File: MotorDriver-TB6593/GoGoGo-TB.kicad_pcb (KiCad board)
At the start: 2 copper layers, 25.4 x 27.9 mm, 21 parts, among them P1 CONN_01X03, P2 CONN_01X04, P3 CONN_01X02, U1 TB6593FNG

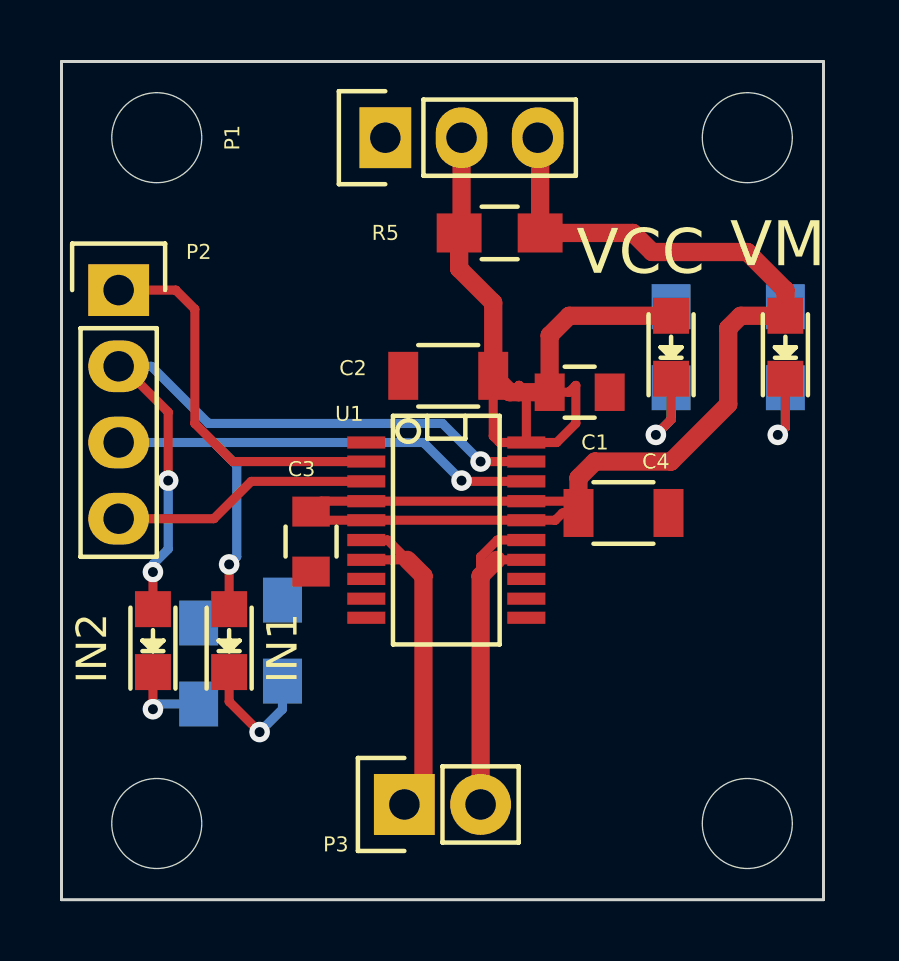
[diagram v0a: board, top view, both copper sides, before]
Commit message: Added via footprint and stitched the planes together.
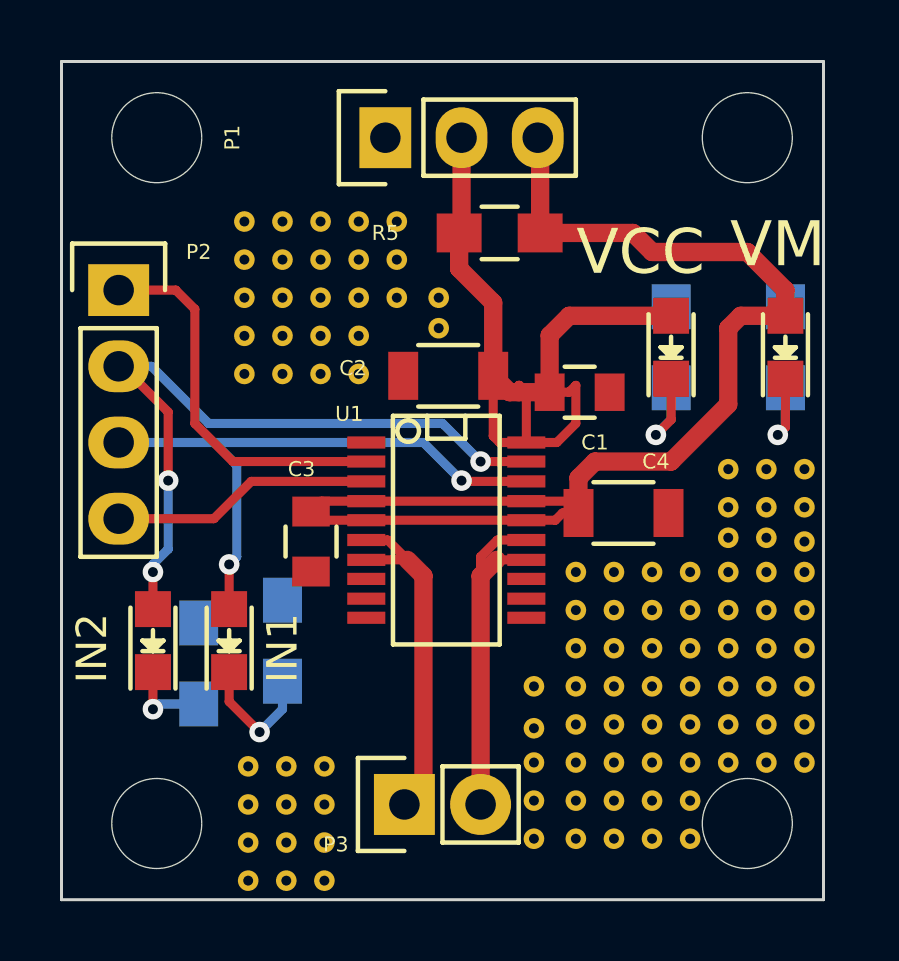
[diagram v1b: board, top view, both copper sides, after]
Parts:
- added REF**111: Via, MotorDriver:Via, F.Cu at (157.5, 110.5)
- added REF**112: Via, MotorDriver:Via, F.Cu at (157.5, 111.8)
- added REF**113: Via, MotorDriver:Via, F.Cu at (157.5, 113.0)
- added REF**114: Via, MotorDriver:Via, F.Cu at (157.5, 114.3)
- added REF**115: Via, MotorDriver:Via, F.Cu at (157.5, 115.6)
- added REF**121: Via, MotorDriver:Via, F.Cu at (158.8, 110.5)
- added REF**122: Via, MotorDriver:Via, F.Cu at (158.8, 111.8)
- added REF**123: Via, MotorDriver:Via, F.Cu at (158.8, 113.0)
- added REF**124: Via, MotorDriver:Via, F.Cu at (158.8, 114.3)
- added REF**125: Via, MotorDriver:Via, F.Cu at (158.8, 115.6)
- added REF**131: Via, MotorDriver:Via, F.Cu at (160.0, 110.5)
- added REF**132: Via, MotorDriver:Via, F.Cu at (160.0, 111.8)
- added REF**133: Via, MotorDriver:Via, F.Cu at (160.0, 113.0)
- added REF**134: Via, MotorDriver:Via, F.Cu at (160.0, 114.3)
- added REF**135: Via, MotorDriver:Via, F.Cu at (160.0, 115.6)
- added REF**141: Via, MotorDriver:Via, F.Cu at (161.3, 110.5)
- added REF**142: Via, MotorDriver:Via, F.Cu at (161.3, 111.8)
- added REF**143: Via, MotorDriver:Via, F.Cu at (161.3, 113.0)
- added REF**144: Via, MotorDriver:Via, F.Cu at (161.3, 114.3)
- added REF**145: Via, MotorDriver:Via, F.Cu at (161.3, 115.6)
- added REF**151: Via, MotorDriver:Via, F.Cu at (162.6, 110.5)
- added REF**1511: Via, MotorDriver:Via, F.Cu at (168.5, 122.2)
- added REF**1512: Via, MotorDriver:Via, F.Cu at (168.5, 123.4)
- added REF**1513: Via, MotorDriver:Via, F.Cu at (168.5, 124.7)
- added REF**1514: Via, MotorDriver:Via, F.Cu at (168.5, 126.0)
- added REF**1515: Via, MotorDriver:Via, F.Cu at (168.5, 127.3)
- added REF**1516: Via, MotorDriver:Via, F.Cu at (168.5, 128.5)
- added REF**1517: Via, MotorDriver:Via, F.Cu at (168.5, 129.8)
- added REF**1518: Via, MotorDriver:Via, F.Cu at (168.5, 131.1)
- added REF**152: Via, MotorDriver:Via, F.Cu at (162.6, 111.8)
- added REF**1521: Via, MotorDriver:Via, F.Cu at (169.8, 122.2)
- added REF**1522: Via, MotorDriver:Via, F.Cu at (169.8, 123.4)
- added REF**1523: Via, MotorDriver:Via, F.Cu at (169.8, 124.7)
- added REF**1524: Via, MotorDriver:Via, F.Cu at (169.8, 126.0)
- added REF**1525: Via, MotorDriver:Via, F.Cu at (169.8, 127.3)
- added REF**1526: Via, MotorDriver:Via, F.Cu at (169.8, 128.5)
- added REF**1527: Via, MotorDriver:Via, F.Cu at (169.8, 129.8)
- added REF**1528: Via, MotorDriver:Via, F.Cu at (169.8, 131.1)
- added REF**153: Via, MotorDriver:Via, F.Cu at (162.6, 113.0)
- added REF**1531: Via, MotorDriver:Via, F.Cu at (171.1, 122.2)
- added REF**1532: Via, MotorDriver:Via, F.Cu at (171.1, 123.4)
- added REF**1533: Via, MotorDriver:Via, F.Cu at (171.1, 124.7)
- added REF**1534: Via, MotorDriver:Via, F.Cu at (171.1, 126.0)
- added REF**1535: Via, MotorDriver:Via, F.Cu at (171.1, 127.3)
- added REF**1536: Via, MotorDriver:Via, F.Cu at (171.1, 128.5)
- added REF**1537: Via, MotorDriver:Via, F.Cu at (171.1, 129.8)
- added REF**1538: Via, MotorDriver:Via, F.Cu at (171.1, 131.1)
- added REF**154: Via, MotorDriver:Via, F.Cu at (164.0, 114.0)
- added REF**1541: Via, MotorDriver:Via, F.Cu at (172.3, 122.2)
- added REF**1542: Via, MotorDriver:Via, F.Cu at (172.3, 123.4)
- added REF**1543: Via, MotorDriver:Via, F.Cu at (172.3, 124.7)
- added REF**1544: Via, MotorDriver:Via, F.Cu at (172.3, 126.0)
- added REF**1545: Via, MotorDriver:Via, F.Cu at (172.3, 127.3)
- added REF**1546: Via, MotorDriver:Via, F.Cu at (172.3, 128.5)
- added REF**1547: Via, MotorDriver:Via, F.Cu at (172.3, 129.8)
- added REF**1548: Via, MotorDriver:Via, F.Cu at (172.3, 131.1)
- added REF**155: Via, MotorDriver:Via, F.Cu at (164.0, 113.0)
- added REF**1551: Via, MotorDriver:Via, F.Cu at (173.6, 122.2)
- added REF**155111: Via, MotorDriver:Via, F.Cu at (157.6, 128.7)
- added REF**155112: Via, MotorDriver:Via, F.Cu at (157.6, 129.9)
- added REF**155113: Via, MotorDriver:Via, F.Cu at (157.6, 131.2)
- added REF**155114: Via, MotorDriver:Via, F.Cu at (157.6, 132.5)
- added REF**155121: Via, MotorDriver:Via, F.Cu at (158.9, 128.7)
- added REF**155122: Via, MotorDriver:Via, F.Cu at (158.9, 129.9)
- added REF**155123: Via, MotorDriver:Via, F.Cu at (158.9, 131.2)
- added REF**155124: Via, MotorDriver:Via, F.Cu at (158.9, 132.5)
- added REF**155131: Via, MotorDriver:Via, F.Cu at (160.1, 128.7)
- added REF**155132: Via, MotorDriver:Via, F.Cu at (160.1, 129.9)
- added REF**155133: Via, MotorDriver:Via, F.Cu at (160.1, 131.2)
- added REF**155134: Via, MotorDriver:Via, F.Cu at (160.1, 132.5)
- added REF**1552: Via, MotorDriver:Via, F.Cu at (173.6, 123.4)
- added REF**1553: Via, MotorDriver:Via, F.Cu at (173.6, 124.7)
- added REF**1554: Via, MotorDriver:Via, F.Cu at (173.6, 126.0)
- added REF**1555: Via, MotorDriver:Via, F.Cu at (173.6, 127.3)
- added REF**1556: Via, MotorDriver:Via, F.Cu at (173.6, 128.5)
- added REF**1557: Via, MotorDriver:Via, F.Cu at (167.1, 129.8)
- added REF**1558: Via, MotorDriver:Via, F.Cu at (167.1, 131.1)
- added REF**1561: Via, MotorDriver:Via, F.Cu at (174.9, 122.2)
- added REF**1562: Via, MotorDriver:Via, F.Cu at (174.9, 123.4)
- added REF**1563: Via, MotorDriver:Via, F.Cu at (174.9, 124.7)
- added REF**1564: Via, MotorDriver:Via, F.Cu at (174.9, 126.0)
- added REF**1565: Via, MotorDriver:Via, F.Cu at (174.9, 127.3)
- added REF**1566: Via, MotorDriver:Via, F.Cu at (174.9, 128.5)
- added REF**1567: Via, MotorDriver:Via, F.Cu at (167.1, 128.5)
- added REF**1568: Via, MotorDriver:Via, F.Cu at (167.1, 127.4)
- added REF**1571: Via, MotorDriver:Via, F.Cu at (176.1, 122.2)
- added REF**1572: Via, MotorDriver:Via, F.Cu at (176.1, 123.4)
- added REF**1573: Via, MotorDriver:Via, F.Cu at (176.1, 124.7)
- added REF**1574: Via, MotorDriver:Via, F.Cu at (176.1, 126.0)
- added REF**1575: Via, MotorDriver:Via, F.Cu at (176.1, 127.3)
- added REF**1576: Via, MotorDriver:Via, F.Cu at (176.1, 128.5)
- added REF**1577: Via, MotorDriver:Via, F.Cu at (167.1, 126.0)
- added REF**1578: Via, MotorDriver:Via, F.Cu at (173.6, 118.7)
- added REF**1581: Via, MotorDriver:Via, F.Cu at (173.6, 121.0)
- added REF**1582: Via, MotorDriver:Via, F.Cu at (174.9, 121.0)
- added REF**1583: Via, MotorDriver:Via, F.Cu at (176.1, 121.2)
- added REF**1584: Via, MotorDriver:Via, F.Cu at (176.1, 120.0)
- added REF**1585: Via, MotorDriver:Via, F.Cu at (174.9, 120.0)
- added REF**1586: Via, MotorDriver:Via, F.Cu at (173.6, 120.0)
- added REF**1587: Via, MotorDriver:Via, F.Cu at (174.9, 118.7)
- added REF**1588: Via, MotorDriver:Via, F.Cu at (176.1, 118.7)
- renumbered REF** to REF**11

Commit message: Did DRC and added silkscreen
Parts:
- moved REF**1566 14.0 mm to (161.3, 125.0)
- moved REF**1576 13.8 mm to (162.4, 127.3)
- moved REF**1548 12.1 mm to (161.3, 126.1)
- moved REF**1556 11.4 mm to (162.4, 126.1)
- moved REF**1547 11.3 mm to (161.3, 127.3)
- moved REF**1546 10.5 mm to (162.4, 125.0)
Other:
- board text added: "G"
- board text added: "PWM"
- board text added: "STBY"
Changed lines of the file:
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@@
 (kicad_pcb (version 4) (host pcbnew 0.201509151501+6198~30~ubuntu14.04.1-product)
   (general
-    (links 132)
+    (links 143)
     (no_connects 0)
     (area 150.669934 103.0431 179.054303 136.10966)
     (thickness 1.6)
-    (drawings 8)
+    (drawings 13)
     (tracks 113)
     (zones 0)
@@
   (layers
     (0 F.Cu signal)
-    (31 B.Cu signal)
-    (32 B.Adhes user)
+    (31 B.Cu signal hide)
+    (32 B.Adhes user hide)
     (33 F.Adhes user)
-    (34 B.Paste user)
+    (34 B.Paste user hide)
     (35 F.Paste user)
-    (36 B.SilkS user)
+    (36 B.SilkS user hide)
     (37 F.SilkS user)
     (38 B.Mask user)
@@
   )
   (setup
-    (last_trace_width 0.1524)
+    (last_trace_width 0.6096)
     (user_trace_width 0.3048)
     (user_trace_width 0.6096)
@@
     (aux_axis_origin 0 0)
     (grid_origin 161.544 117.856)
-    (visible_elements FFFEFF7F)
+    (visible_elements FFFEFB3F)
     (pcbplotparams
       (layerselection 0x010fc_80000001)
@@
   )
   (module MotorDriver:Via (layer F.Cu)
-    (at 172.339 131.064)
+    (at 161.29 126.111)
     (fp_text reference REF**1548 (at 0 1) (layer F.SilkS) hide
       (effects (font (size 1 1) (thickness 0.15)))
@@
   )
   (module MotorDriver:Via (layer F.Cu)
-    (at 172.339 129.794)
+    (at 161.29 127.254)
     (fp_text reference REF**1547 (at 0 1) (layer F.SilkS) hide
       (effects (font (size 1 1) (thickness 0.15)))
@@
   )
   (module MotorDriver:Via (layer F.Cu)
-    (at 176.149 128.524)
+    (at 162.433 127.254)
     (fp_text reference REF**1576 (at 0 1) (layer F.SilkS) hide
       (effects (font (size 1 1) (thickness 0.15)))
@@
   )
   (module MotorDriver:Via (layer F.Cu)
-    (at 174.879 128.524)
+    (at 161.29 124.968)
     (fp_text reference REF**1566 (at 0 1) (layer F.SilkS) hide
       (effects (font (size 1 1) (thickness 0.15)))
@@
   )
   (module MotorDriver:Via (layer F.Cu)
-    (at 173.609 128.524)
+    (at 162.433 126.111)
     (fp_text reference REF**1556 (at 0 1) (layer F.SilkS) hide
       (effects (font (size 1 1) (thickness 0.15)))
@@
   )
   (module MotorDriver:Via (layer F.Cu)
-    (at 172.339 128.524)
+    (at 162.433 124.968)
     (fp_text reference REF**1546 (at 0 1) (layer F.SilkS) hide
       (effects (font (size 1 1) (thickness 0.15)))
@@
     (tags "capacitor 1206")
     (attr smd)
-    (fp_text reference C4 (at 1.0795 -1.7145) (layer F.SilkS)
+    (fp_text reference C4 (at 2.2225 -1.8415) (layer F.SilkS)
       (effects (font (size 0.5 0.5) (thickness 0.1)))
     )
@@
     (tags "capacitor 0805")
     (attr smd)
-    (fp_text reference C1 (at 0.508 1.6764) (layer F.SilkS)
+    (fp_text reference C1 (at 0.635 -1.4986) (layer F.SilkS)
       (effects (font (size 0.5 0.5) (thickness 0.1)))
     )
@@
     (tags "capacitor 1206")
     (attr smd)
-    (fp_text reference C2 (at 3.175 0.254 180) (layer F.SilkS)
+    (fp_text reference C2 (at 1.5875 1.7145 180) (layer F.SilkS)
       (effects (font (size 0.5 0.5) (thickness 0.1)))
     )
@@
     (descr "Through hole pin header")
     (tags "pin header")
-    (fp_text reference P2 (at 2.667 -1.27) (layer F.SilkS)
+    (fp_text reference P2 (at -1.27 -2.286) (layer F.SilkS)
       (effects (font (size 0.5 0.5) (thickness 0.1)))
     )
@@
     (tags "CMS SSOP SMD")
     (attr smd)
-    (fp_text reference U1 (at -3.8735 3.2385 360) (layer F.SilkS)
+    (fp_text reference U1 (at -3.302 2.54 360) (layer F.SilkS)
       (effects (font (size 0.5 0.5) (thickness 0.1)))
     )
@@
       (net 1 GND) (zone_connect 2))
   )
-  (gr_text IN1 (at 158.75 124.714 90) (layer F.SilkS)
+  (gr_text PWM (at 156.591 113.157) (layer F.SilkS)
+    (effects (font (size 0.762 0.762) (thickness 0.1524)))
+  )
+  (gr_text IN2 (at 155.829 115.443) (layer F.SilkS)
+    (effects (font (size 0.762 0.762) (thickness 0.1524)))
+  )
+  (gr_text IN1 (at 156.083 117.729) (layer F.SilkS)
+    (effects (font (size 0.762 0.762) (thickness 0.1524)))
+  )
+  (gr_text STBY (at 156.21 120.396) (layer F.SilkS)
+    (effects (font (size 0.762 0.762) (thickness 0.1524)))
+  )
+  (gr_text G (at 159.639 108.077) (layer F.SilkS)
+    (effects (font (size 1.016 1.016) (thickness 0.2032)))
+  )
+  (gr_text IN1 (at 158.75 124.46 90) (layer F.SilkS)
     (effects (font (size 1.016 1.016) (thickness 0.2032)))
   )
@@
     (effects (font (size 1.016 1.016) (thickness 0.2032)))
   )
-  (gr_text VM (at 175.26 111.252) (layer F.SilkS)
-    (effects (font (size 1.5 1.5) (thickness 0.3)))
-  )
-  (gr_text VCC (at 170.688 111.506) (layer F.SilkS)
-    (effects (font (size 1.5 1.5) (thickness 0.3)))
+  (gr_text VM (at 175.514 111.633) (layer F.SilkS)
+    (effects (font (size 1.016 1.016) (thickness 0.2032)))
+  )
+  (gr_text VCC (at 171.45 111.506) (layer F.SilkS)
+    (effects (font (size 1.016 1.016) (thickness 0.2032)))
   )
   (gr_line (start 151.384 133.096) (end 176.784 133.096) (layer Edge.Cuts) (width 0.1))

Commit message: Added previous commit # for tracking PCBs
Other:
- board text added: "GoGoGo Motor Driver Board Commit #: b2918eb"
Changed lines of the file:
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@@
     (links 143)
     (no_connects 0)
-    (area 150.669934 103.0431 179.054303 136.10966)
+    (area 150.669934 103.0431 180.42402 136.10966)
     (thickness 1.6)
-    (drawings 13)
+    (drawings 14)
     (tracks 113)
     (zones 0)
@@
   (page A4)
   (layers
-    (0 F.Cu signal)
-    (31 B.Cu signal hide)
-    (32 B.Adhes user hide)
-    (33 F.Adhes user)
-    (34 B.Paste user hide)
-    (35 F.Paste user)
-    (36 B.SilkS user hide)
-    (37 F.SilkS user)
+    (0 F.Cu signal hide)
+    (31 B.Cu signal)
+    (32 B.Adhes user)
+    (33 F.Adhes user hide)
+    (34 B.Paste user)
+    (35 F.Paste user hide)
+    (36 B.SilkS user)
+    (37 F.SilkS user hide)
     (38 B.Mask user)
-    (39 F.Mask user)
-    (40 Dwgs.User user)
+    (39 F.Mask user hide)
+    (40 Dwgs.User user hide)
     (41 Cmts.User user)
     (42 Eco1.User user)
@@
   )
   (setup
-    (last_trace_width 0.6096)
+    (last_trace_width 0.1524)
     (user_trace_width 0.3048)
     (user_trace_width 0.6096)
@@
     (aux_axis_origin 0 0)
     (grid_origin 161.544 117.856)
-    (visible_elements FFFEFB3F)
+    (visible_elements FFFEBD5F)
     (pcbplotparams
       (layerselection 0x010fc_80000001)
@@
     (tags "resistor 0805")
     (attr smd)
-    (fp_text reference R1 (at 0 2.1 270) (layer B.SilkS)
+    (fp_text reference R1 (at 1.778 1.397 270) (layer B.SilkS)
       (effects (font (size 0.5 0.5) (thickness 0.1)) (justify mirror))
     )
@@
     (tags "resistor 0805")
     (attr smd)
-    (fp_text reference R2 (at 0 2.1 270) (layer B.SilkS)
+    (fp_text reference R2 (at 1.905 1.651 270) (layer B.SilkS)
       (effects (font (size 0.5 0.5) (thickness 0.1)) (justify mirror))
     )
@@
     (tags "resistor 0805")
     (attr smd)
-    (fp_text reference R3 (at 0 2.1 270) (layer B.SilkS)
+    (fp_text reference R3 (at -0.635 -1.651 270) (layer B.SilkS)
       (effects (font (size 0.5 0.5) (thickness 0.1)) (justify mirror))
     )
@@
     (tags "resistor 0805")
     (attr smd)
-    (fp_text reference R4 (at 0 2.1 270) (layer B.SilkS)
+    (fp_text reference R4 (at 0.381 1.651 270) (layer B.SilkS)
       (effects (font (size 0.5 0.5) (thickness 0.1)) (justify mirror))
     )
@@
       (net 1 GND) (zone_connect 2))
   )
+  (gr_text "GoGoGo\nMotor Driver Board\nCommit #: b2918eb" (at 169.799 119.38) (layer B.SilkS)
+    (effects (font (size 1.016 1.016) (thickness 0.2032)) (justify left mirror))
+  )
   (gr_text PWM (at 156.591 113.157) (layer F.SilkS)
